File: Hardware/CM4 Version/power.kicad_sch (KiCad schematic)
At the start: 17 parts, among them IC1 TPS62111RSAT, J2 USB_C_Receptacle_USB2.0, J3 Conn_01x02, Q1 AO3401A

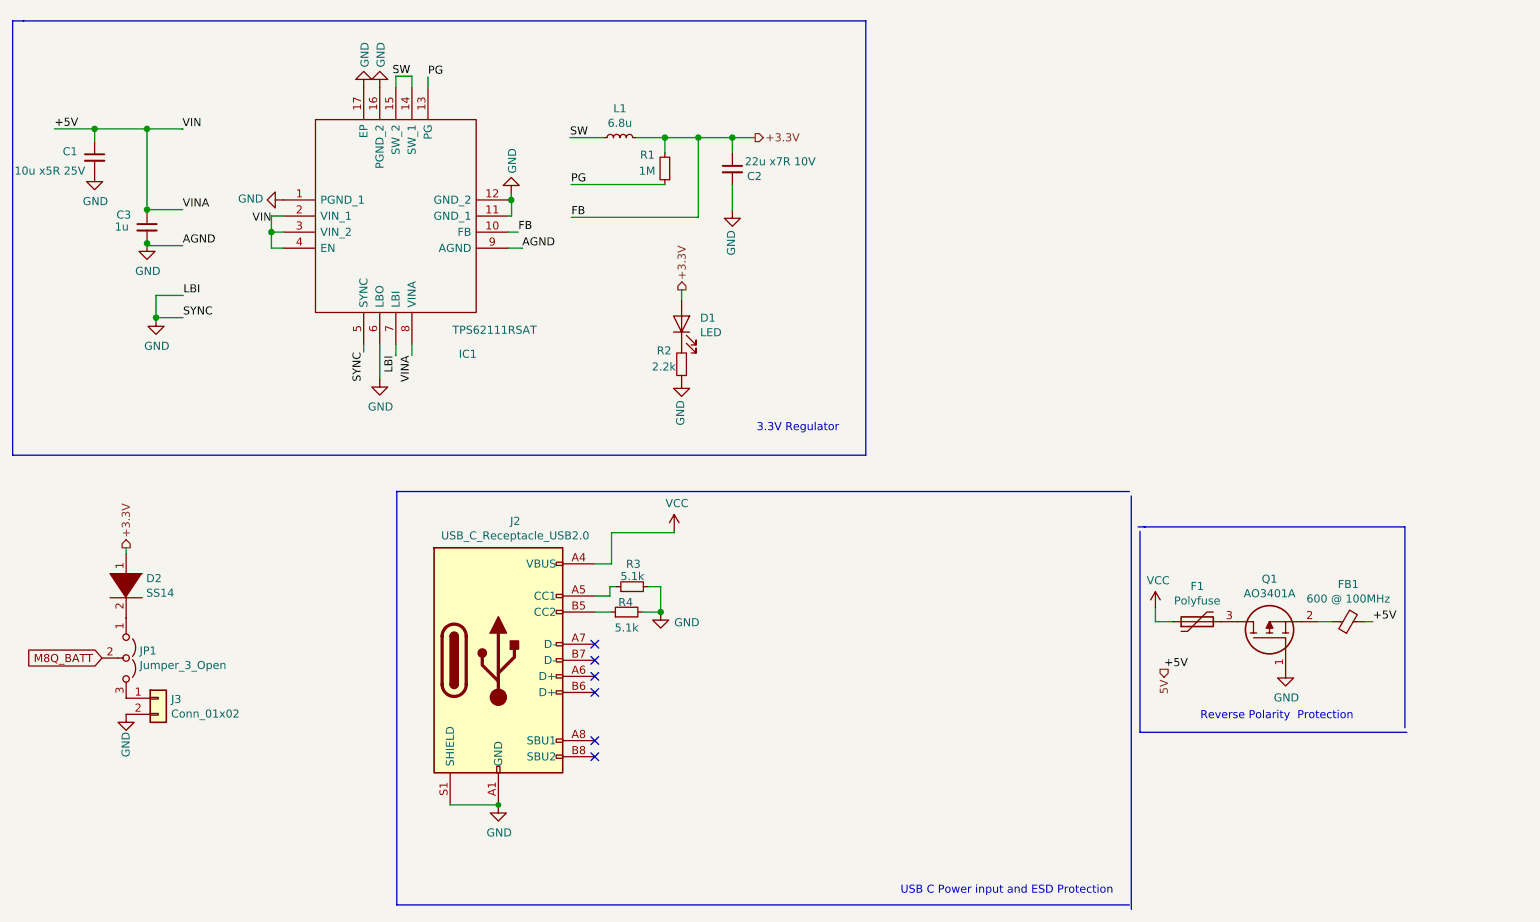
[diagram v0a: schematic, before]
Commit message: Remove CM4-Backups
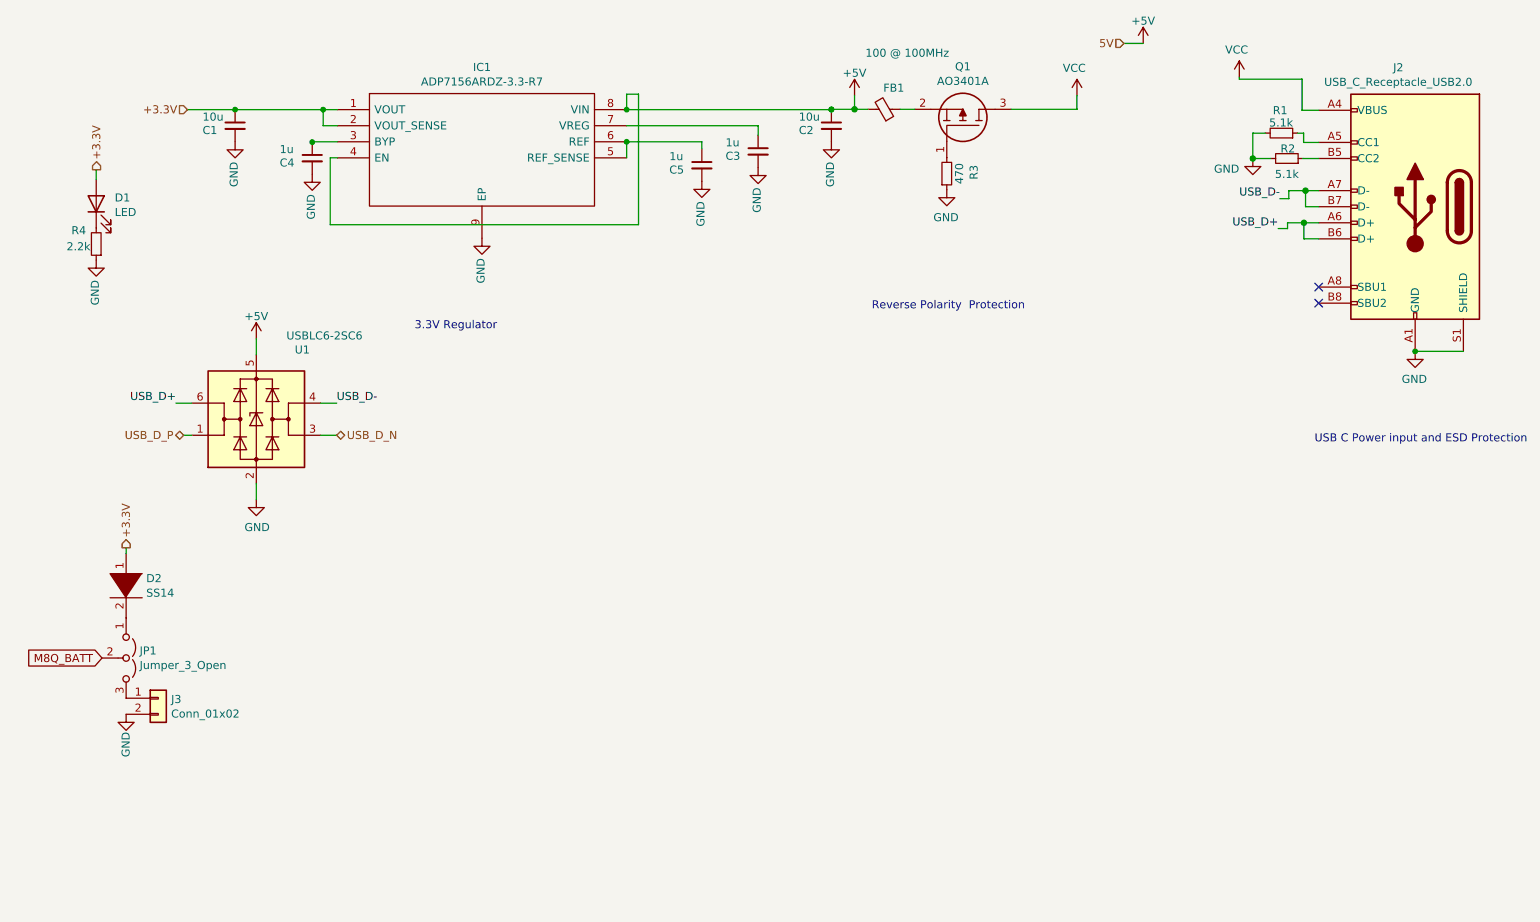
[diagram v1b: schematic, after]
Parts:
- removed F1: Polyfuse, Fuse:Fuse_1206_3216Metric, symbol Device:Polyfuse
- removed IC1: TPS62111RSAT, SamacSys_Parts:QFN65P400X400X100-17N-D, symbol SamacSys_Parts:TPS62111RSAT
- removed L1: 6.8u, Inductor_SMD:L_TDK_SLF7032, symbol Device:L_Small
- added C4, C5: 1u, Capacitor_SMD:C_0603_1608Metric, symbol Device:C_Small
- added IC1: ADP7156ARDZ-3.3-R7, SamacSys_Parts:SOIC127P600X175-9N, symbol SamacSys_Parts:ADP7156ARDZ-3.3-R7
- added U1: USBLC6-2SC6, Package_TO_SOT_SMD:SOT-23-6, symbol Power_Protection:USBLC6-2SC6
- C1: value 10u x5R 25V -> 10u; footprint Capacitor_SMD:C_1210_3225Metric -> Capacitor_SMD:C_0603_1608Metric; Digi-Key_PN 1276-1854-2-ND -> (none); Digikey Link https://www.digikey.co.uk/en/products/detail/samsung-electr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 -> (none); LCSC Part # (none) -> C19702; Manufacturer_Part_Number CL32B106KAJNNNE -> (none)
- C2: value 22u x7R 10V -> 10u; footprint Capacitor_SMD:C_1210_3225Metric -> Capacitor_SMD:C_0603_1608Metric; Digi-Key_PN 311-2057-2-ND -> (none); Digikey Link https://www.digikey.co.uk/en/products/detail/yageo/CC1210MK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 -> (none); LCSC Part # (none) -> C19702; Manufacturer_Part_Number CL32A226KAJNNNE -> (none)
- C3: footprint Capacitor_SMD:C_0805_2012Metric -> Capacitor_SMD:C_0603_1608Metric; Digi-Key_PN 445-CGA4J1X8L1H105K125ACTR-ND -> (none); Digikey Link https://www.digikey.co.uk/en/products/detail/tdk-corporatio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 -> (none); LCSC Part # (none) -> C15849; Seeed SKU 302010003 -> (none)
- D1: LCSC Part # (none) -> C72043; Seeed SKU 304090042 -> (none)
- D2: Digi-Key_PN SS14CT-ND -> (none)
- FB1: value 600 @ 100MHz -> 100 @ 100MHz; footprint Inductor_SMD:L_0805_2012Metric -> Inductor_SMD:L_0603_1608Metric
- J2: LCSC Part # (none) -> C165948
- Q1: Digi-Key_PN 785-1001-2-ND -> (none); LCSC Part # C15127 -> (none)
- R1: value 1M -> 5.1k; footprint Resistor_SMD:R_0805_2012Metric -> Resistor_SMD:R_1206_3216Metric; LCSC Part # (none) -> C26033; Seeed SKU 301012157 -> 301010495
- R2: value 2.2k -> 5.1k; footprint Resistor_SMD:R_0603_1608Metric -> Resistor_SMD:R_1206_3216Metric; LCSC Part # (none) -> C26033; Seeed SKU 301010124 -> 301010495
- R3: value 5.1k -> 470
- R4: value 5.1k -> 2.2k; footprint Resistor_SMD:R_1206_3216Metric -> Resistor_SMD:R_0603_1608Metric; LCSC Part # C26033 -> C4190; Seeed SKU 301010495 -> (none)
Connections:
- net PG is gone; now on an unnamed net: R1.1
- net +3.3V: now also C1.1, IC1.1 (VOUT), IC1.2 (VOUT_SENSE); no longer C2.1, R1.2
- net GND: now also R1.2, R2.2, R3.1, R4.1, C4.2, C5.2, IC1.9 (EP), U1.2 (GND); no longer Q1.1, R2.1, R3.2, R4.2
- net VCC: now also Q1.3
- net at D1.1 (K): now also R4.2; no longer R2.2
- net at J2.A5 (CC1): no longer R3.1
- net at J2.B5 (CC2): now also R2.1; no longer R4.1
- net USB_D+: now reaches J2.A6 (D+)
- net USB_D+: now also J2.B6 (D+), U1.6 (I/O1)
- net USB_D-: now reaches J2.A7 (D-)
- net USB_D-: now also J2.B7 (D-), U1.4 (I/O2)
- removed net 5V: C1.1, C3.1, FB1.2
- new net: C4.1, IC1.3 (BYP)
- new net: Q1.1, R3.2
- new net: C3.1, IC1.7 (VREG)
- new net: C5.1, IC1.5 (REF_SENSE), IC1.6 (REF)
- new net +5V: C2.1, FB1.2, IC1.4 (EN), IC1.8 (VIN), U1.5 (VBUS)
- new net USB_D_N: U1.3 (I/O2)
- new net USB_D_P: U1.1 (I/O1)
- no-connect marks 6 -> 2
